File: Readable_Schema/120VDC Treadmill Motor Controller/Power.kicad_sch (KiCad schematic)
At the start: 7 parts, among them J1 TB005-762-03BE, J6 TB0011-350-03BE, K1 T9GV1L14-24, U8 RAC05E-05SKT

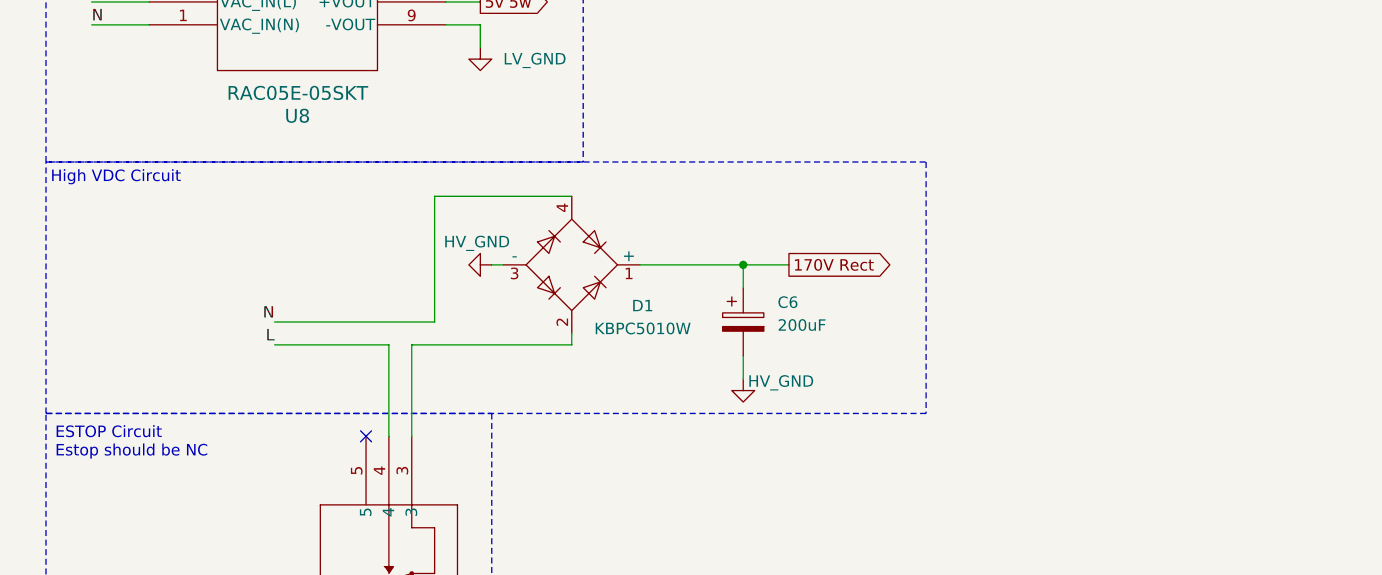
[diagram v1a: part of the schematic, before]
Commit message: -Removed brake resistor subcircuit -Worked up bus cap to 4x 820uF 400V caps -changed the fets to 600V 49A 60mOhm RdsON --------------------------------------------- -need different isolated power supplies --May want to consider a bootstrap circuit since we wont be needing 100% duty cycle -need to resize gate resistors -Need to change out bridge rectifier to be vertical for ease of mounting heatsink
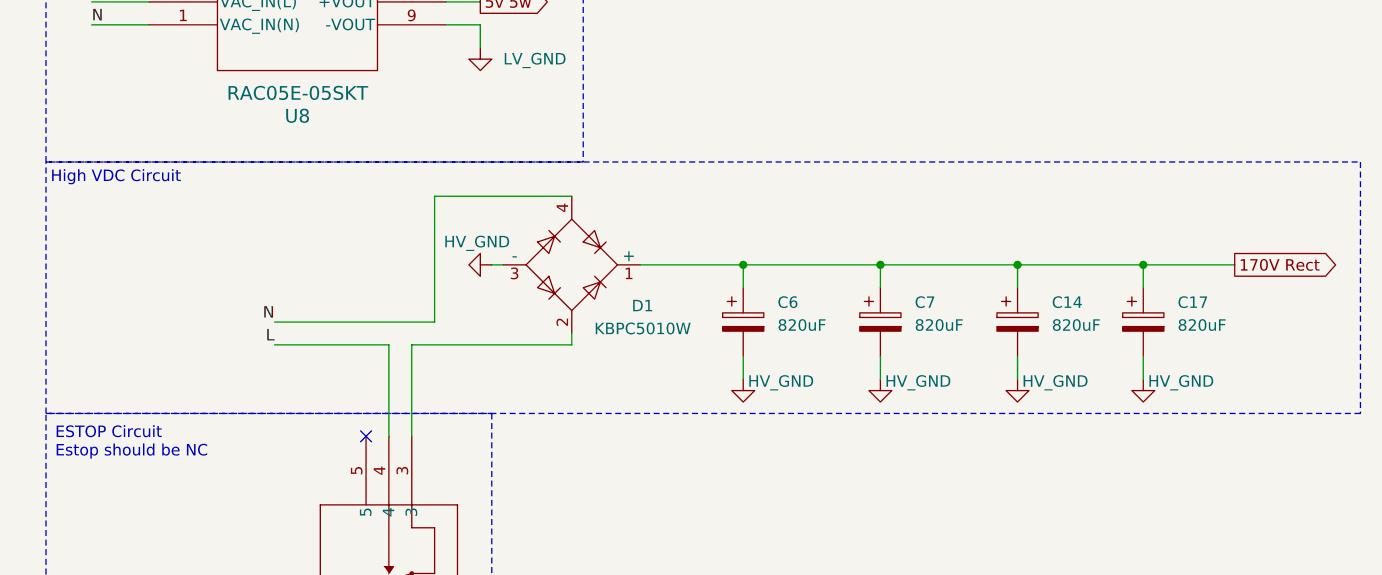
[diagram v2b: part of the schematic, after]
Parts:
- added C14, C17, C7: 820uF, Treadmill_Feet:CHEMI-VSN_A45, symbol Device:C_Polarized
- C6: value 200uF -> 820uF; footprint Capacitor_THT:CP_Radial_D18.0mm_P7.50mm -> Treadmill_Feet:CHEMI-VSN_A45
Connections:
- net 170V Rect: now also C14.1, C17.1, C7.1
- net HV_GND: now also C14.2, C17.2, C7.2

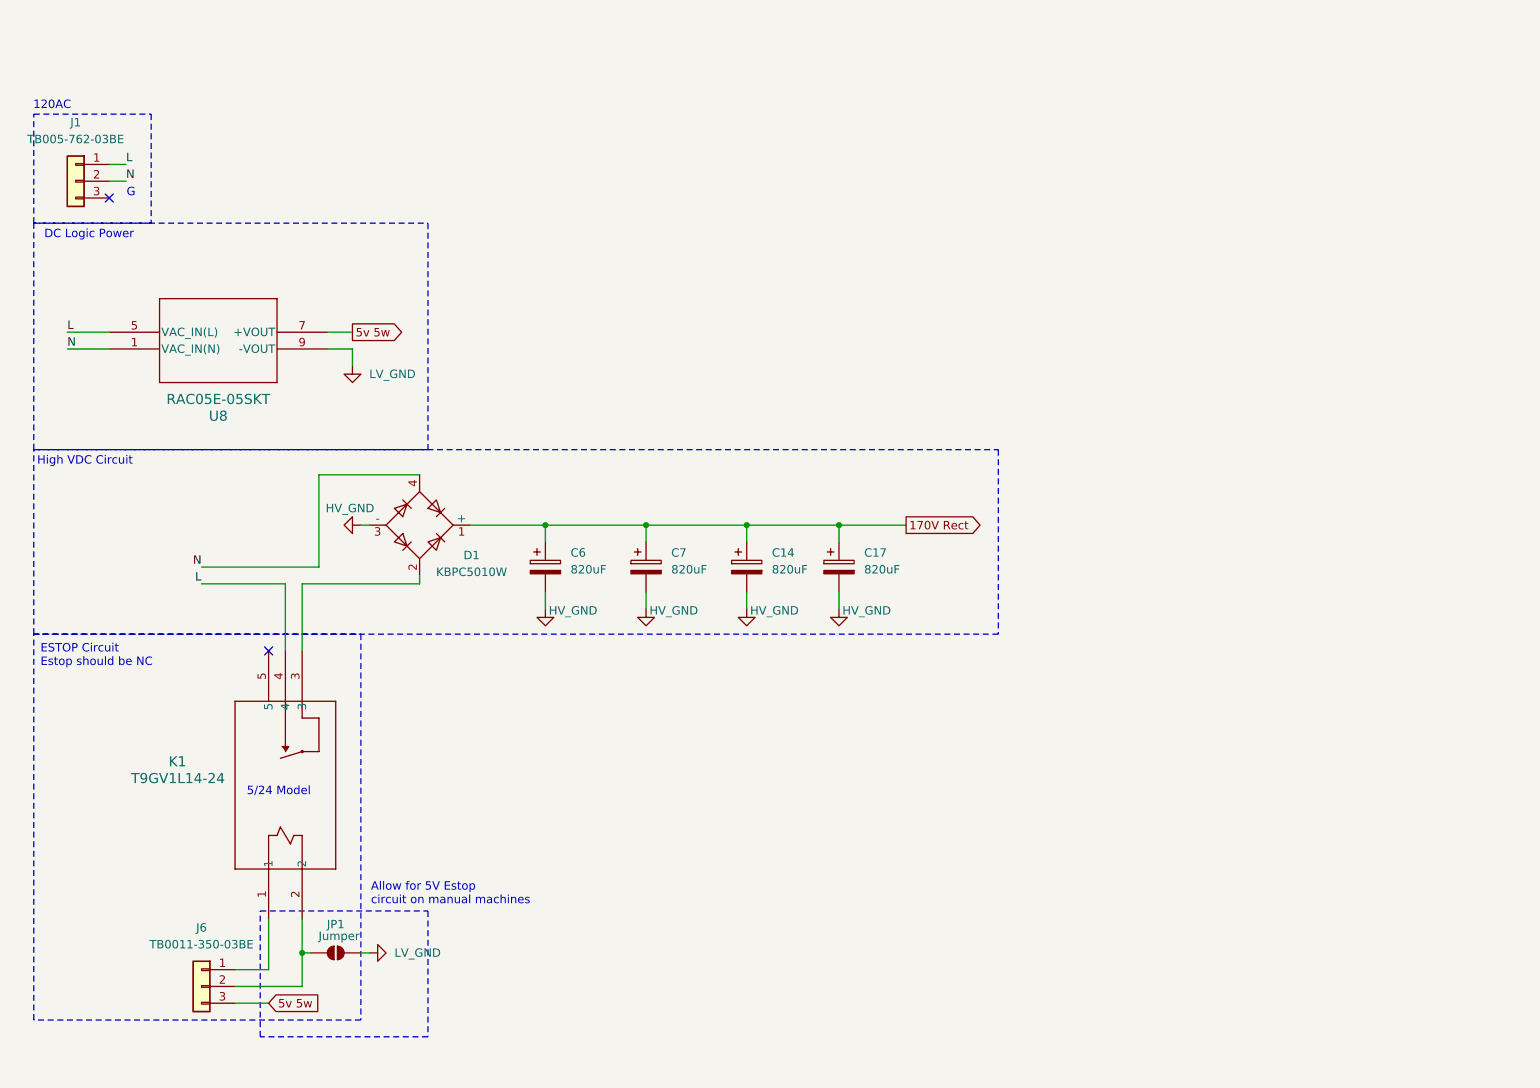
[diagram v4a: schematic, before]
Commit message: -Worked on getting the precharge circuit working --Picked a gate driver --Picked Ron and Roff resistors
-Still need to work through the board logic for turning off the gate when the caps reach 170vdc
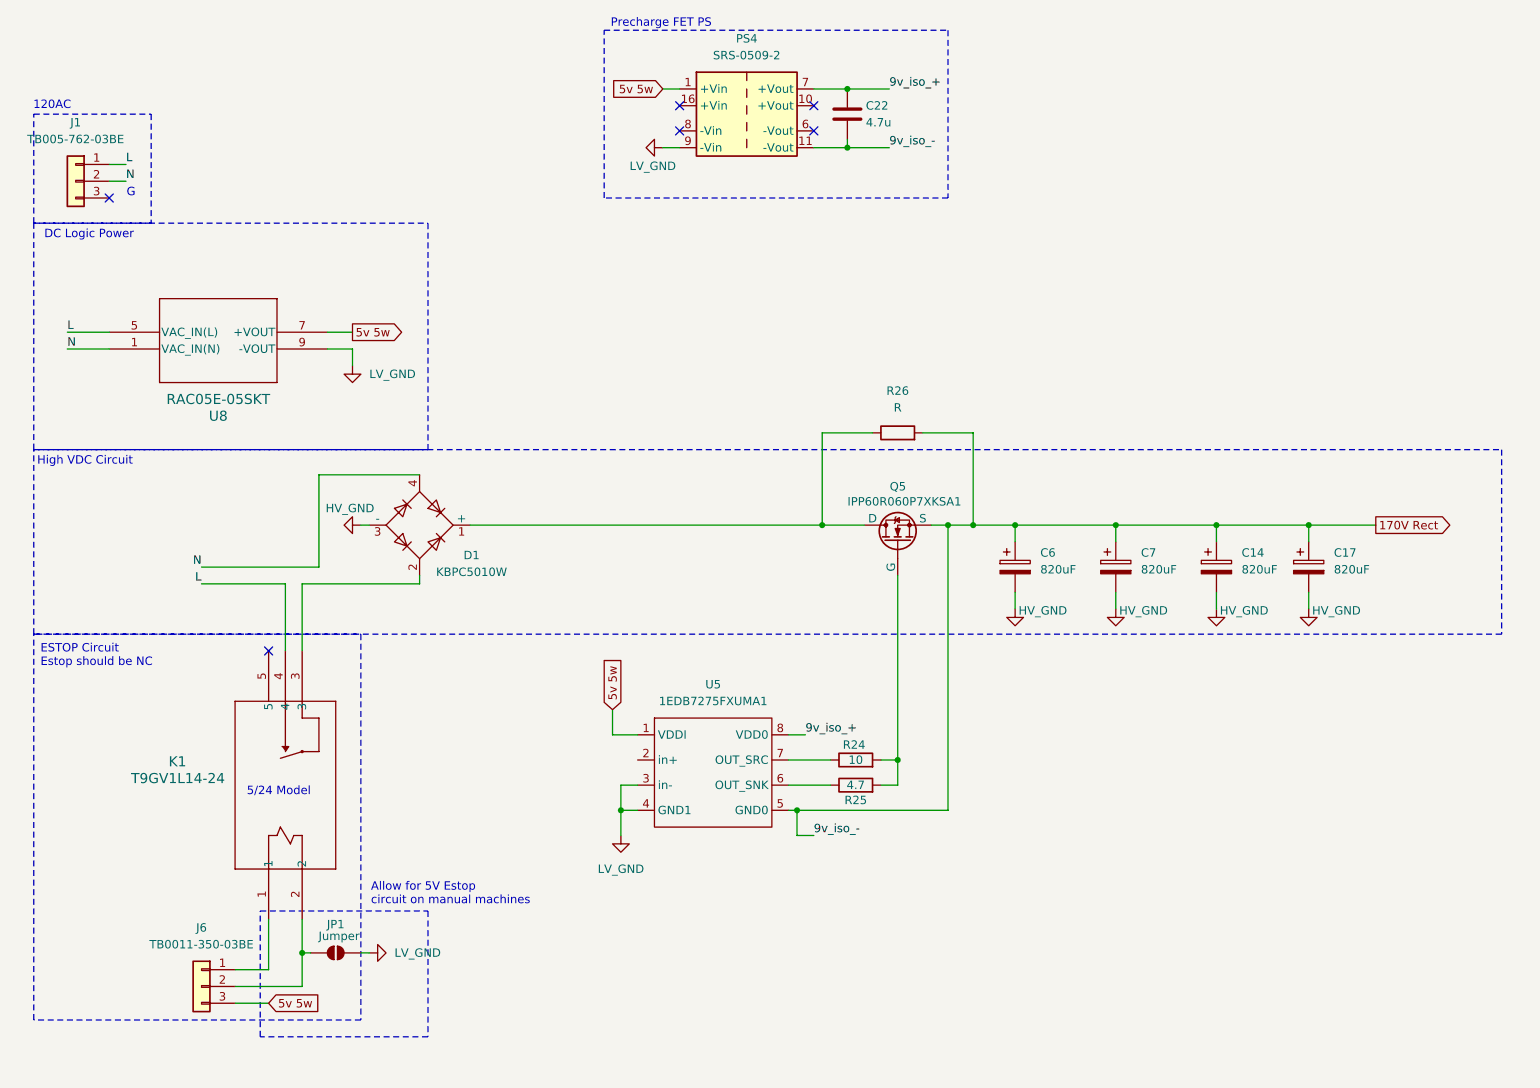
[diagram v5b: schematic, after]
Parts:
- added C22: 4.7u, Capacitor_SMD:C_0402_1005Metric_Pad0.74x0.62mm_HandSolder, symbol Device:C
- added PS4: SRS-0509-2, Footprints_TMC:SRS-0515 DIP-16_W7.62mm, symbol Treadmill_Comp:SRS-0515-2
- added Q5: IPP60R060P7XKSA1, Package_TO_SOT_THT:TO-220-3_Vertical, symbol Simulation_SPICE:NMOS
- added R24: 10, Resistor_SMD:R_0201_0603Metric_Pad0.64x0.40mm_HandSolder, symbol Device:R
- added R25: 4.7, Resistor_SMD:R_0201_0603Metric_Pad0.64x0.40mm_HandSolder, symbol Device:R
- added R26: R, symbol Device:R
- added U5: 1EDB7275FXUMA1, Treadmill_Feet:Infineon_PG-DSO-8-41, symbol Treadmill_Comp:1EDB7275FXUMA1
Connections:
- net 170V Rect: now also C22.2, PS4.11 (-Vout), Q5.3 (S), R26.2, U5.5 (GND0); no longer D1.1 (+)
- net 5v 5w: now also PS4.1 (+Vin), U5.1 (VDDI)
- net LV_GND: now also PS4.9 (-Vin), U5.3 (in-), U5.4 (GND1)
- new net: R25.1, U5.6 (OUT_SNK)
- new net: Q5.2 (G), R24.2, R25.2
- new net: R24.1, U5.7 (OUT_SRC)
- new net: D1.1 (+), Q5.1 (D), R26.1
- new net 9v_iso_+: C22.1, PS4.7 (+Vout), U5.8 (VDD0)
- no-connect marks 2 -> 6
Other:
- note added: "Precharge FET PS"
- moved on the sheet: C14, C17, C6, C7

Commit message: -Changed the precharge circuit gate driver to the TP5I3 --This gate driver provides its own 10v isolated PS, which saves a lot of room
-changed the schottky for the pi pico to a smd equivalent.
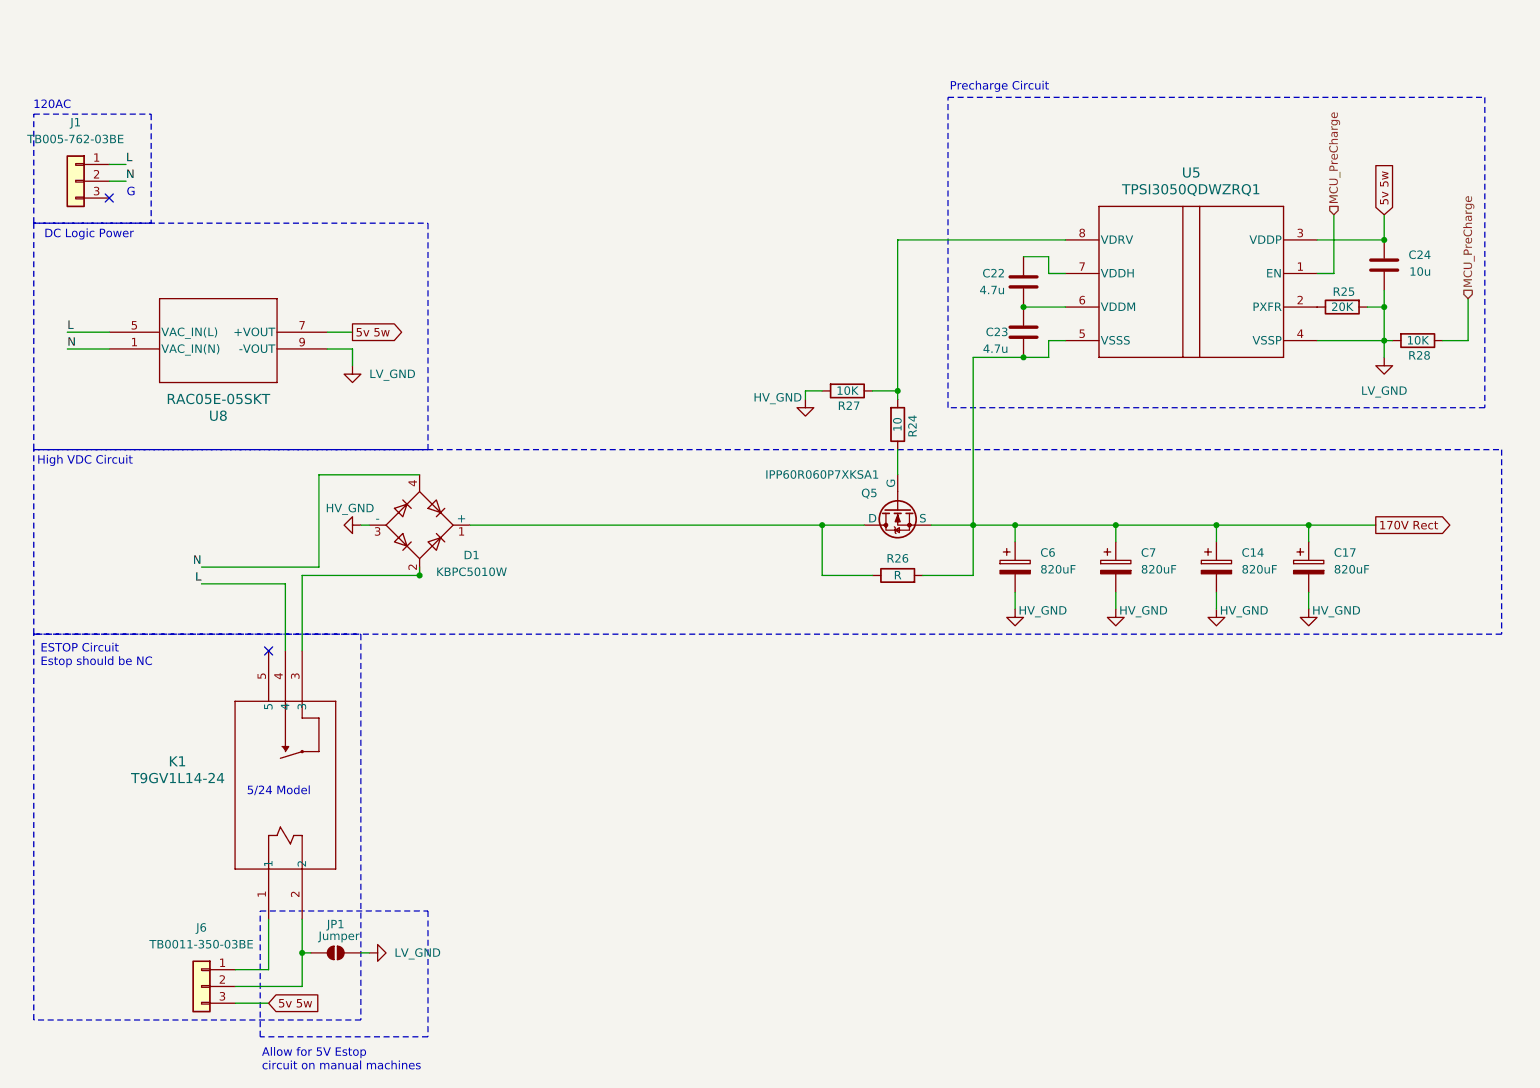
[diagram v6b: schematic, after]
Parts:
- removed PS4: SRS-0509-2, Footprints_TMC:SRS-0515 DIP-16_W7.62mm, symbol Treadmill_Comp:SRS-0515-2
- removed U5: 1EDB7275FXUMA1, Treadmill_Feet:Infineon_PG-DSO-8-41, symbol Treadmill_Comp:1EDB7275FXUMA1
- added C23: 4.7u, Capacitor_SMD:C_0402_1005Metric_Pad0.74x0.62mm_HandSolder, symbol Device:C
- added C24: 10u, Capacitor_SMD:C_0402_1005Metric_Pad0.74x0.62mm_HandSolder, symbol Device:C
- added R27, R28: 10K, Resistor_SMD:R_0201_0603Metric_Pad0.64x0.40mm_HandSolder, symbol Device:R
- added U5: TPSI3050QDWZRQ1, Treadmill_Feet:DWZ0008A-IPC_A, symbol Treadmill_Comp:TPSI3050QDWZRQ1
- R25: value 4.7 -> 20K
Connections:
- net 170V Rect: now also C23.2, U5.5 (VSSS); no longer C22.2
- net 5v 5w: now also C24.1, U5.3 (VDDP)
- net HV_GND: now also R27.2
- net LV_GND: now also R25.2, C24.2, R28.2, U5.4 (VSSP)
- net at R25.1: now also U5.2 (PXFR)
- net at R24.1: now also Q5.2 (G)
- net 9v_iso_+: no longer names the net of C22.1
- net 9v_iso_+: now also U5.7 (VDDH)
- new net: C22.2, C23.1, U5.6 (VDDM)
- new net: R24.2, R27.1, U5.8 (VDRV)
- new net MCU_PreCharge: R28.1, U5.1 (EN)
- no-connect marks 6 -> 2
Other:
- note added: "Precharge Circuit"
- note removed: "Precharge FET PS"
- moved on the sheet: Q5, R24, R26

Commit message: -Added some caps directly next to the isolated power supplies -Resized some gate resistors to be 1206 -chose a precharge circuit resistor HSA50330RJ -pulled caps low so they drain to a relatively safe level within 15 min
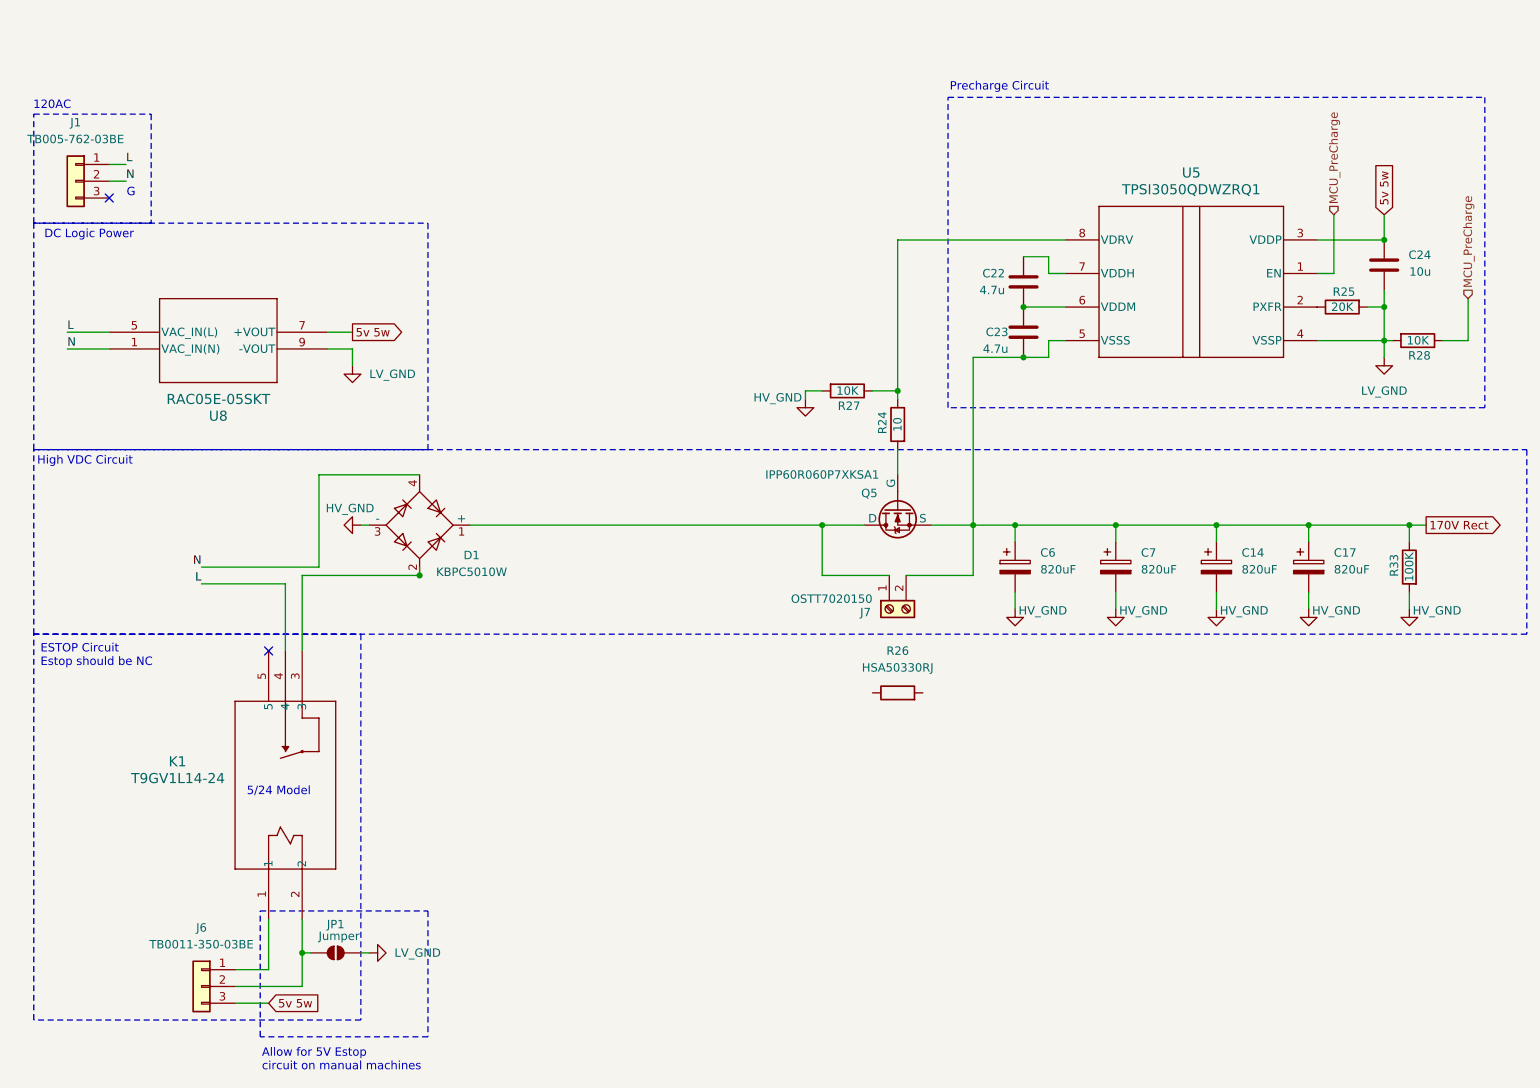
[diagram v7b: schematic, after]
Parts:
- added J7: OSTT7020150, Treadmill_Feet:CONN2_OSTT7020150_OST, symbol Connector:Screw_Terminal_01x02
- added R33: HVCB2512FKC100K, Resistor_SMD:R_2512_6332Metric_Pad1.40x3.35mm_HandSolder, symbol Device:R
- R24: footprint Resistor_SMD:R_0201_0603Metric_Pad0.64x0.40mm_HandSolder -> Resistor_SMD:R_1206_3216Metric_Pad1.30x1.75mm_HandSolder
- R26: value R -> HSA50330RJ
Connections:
- net 170V Rect: now also J7.2 (Pin_2), R33.1; no longer R26.2
- net HV_GND: now also R33.2
- net at R27.1, U5.8 (VDRV): now also R24.1; no longer R24.2
- net at D1.1 (+), Q5.1 (D): now also J7.1 (Pin_1); no longer R26.1
- net at Q5.2 (G): now also R24.2; no longer R24.1
